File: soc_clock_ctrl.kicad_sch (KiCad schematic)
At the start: 19 parts, among them U1 MCIMX6Y2DVM09AB

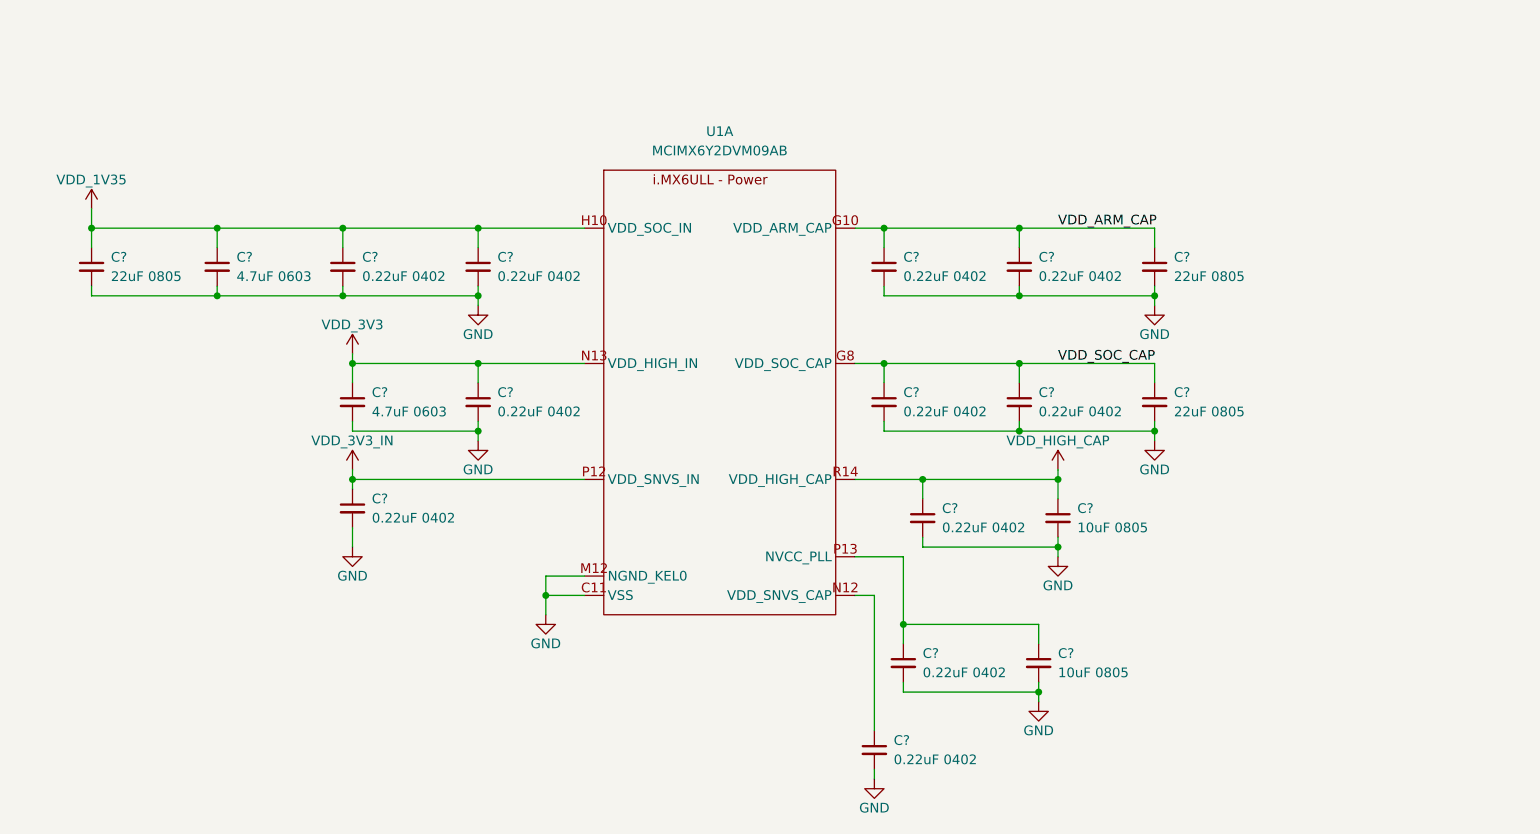
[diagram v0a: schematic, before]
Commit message: Core power; clock/ctrl
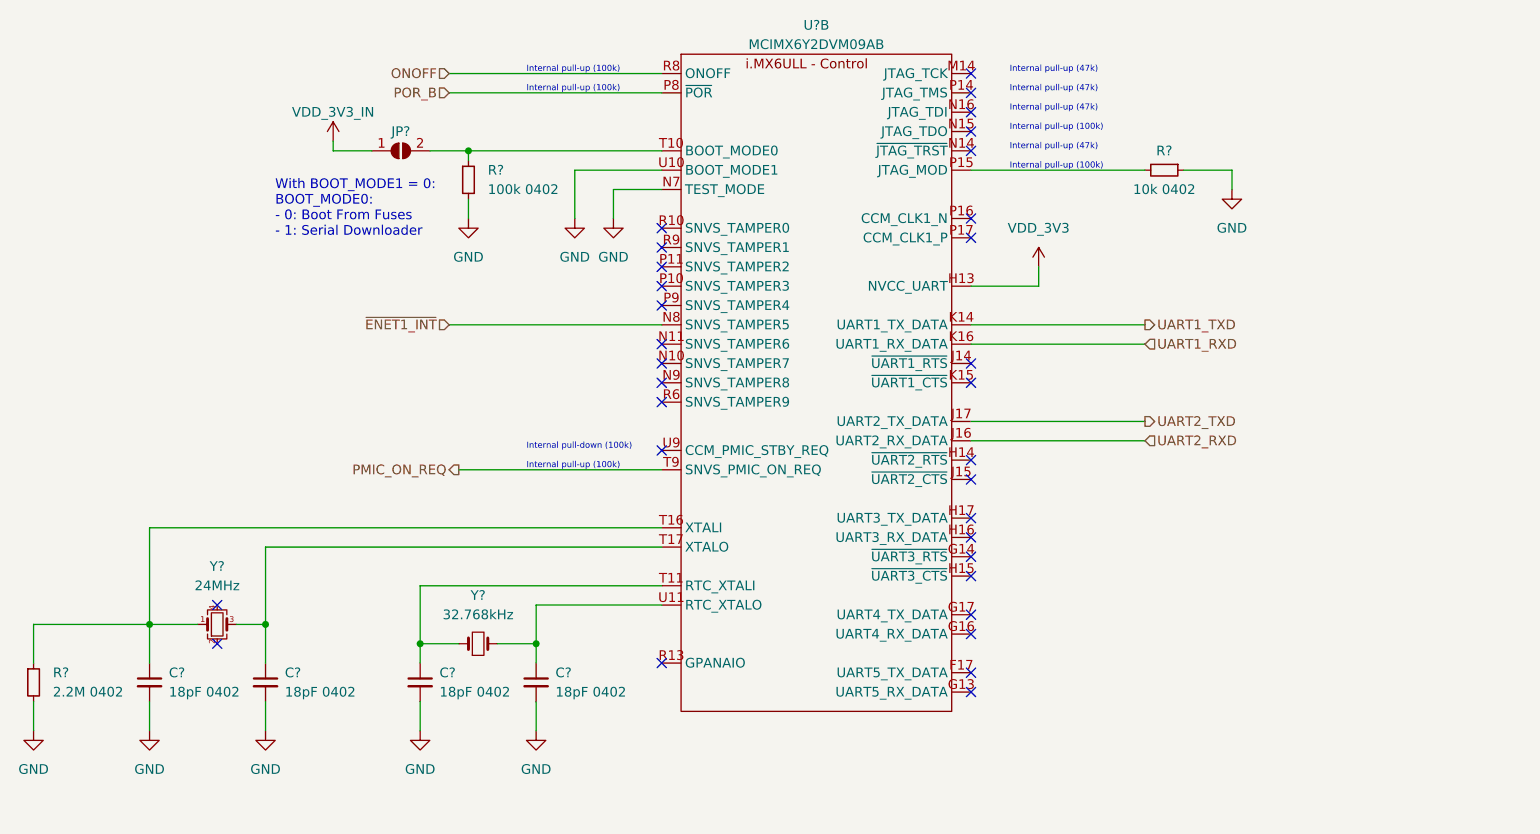
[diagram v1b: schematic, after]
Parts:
- removed C? (x11): 0.22uF 0402, symbol Device:C_Small
- removed C? (x2): 10uF 0805, symbol Device:C_Small
- removed C? (x2): 4.7uF 0603, symbol Device:C_Small
- removed C? (x3): 22uF 0805, symbol Device:C_Small
- removed U1: MCIMX6Y2DVM09AB, symbol catfood:MCIMX6YxxVMxxxx
- added C? (x4): 18pF 0402, symbol Device:C_Small
- added JP?: SolderJumper_2_Open, symbol Jumper:SolderJumper_2_Open
- added R?: 10k 0402, symbol Device:R_Small
- added R?: 2.2M 0402, symbol Device:R_Small
- added R?: 100k 0402, symbol Device:R_Small
- added U?: MCIMX6Y2DVM09AB, symbol catfood:MCIMX6YxxVMxxxx
- added Y?: 24MHz, symbol Device:Crystal_GND24_Small
- added Y?: 32.768kHz, symbol Device:Crystal_Small
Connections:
- net GND: now also C?.2, C?.2, C?.2, C?.2, R?.1, R?.2, R?.2, U?.N7 (TEST_MODE), U?.U10 (BOOT_MODE1)
- net VDD_3V3: now also U?.H13 (NVCC_UART)
- net VDD_3V3_IN: now also JP?.1 (A)
- new net: C?.1, R?.1, U?.T16 (XTALI), Y?.1
- new net: C?.1, U?.T17 (XTALO), Y?.3
- new net: R?.2, U?.P15 (JTAG_MOD)
- new net: JP?.2 (B), R?.1, U?.T10 (BOOT_MODE0)
- new net: C?.1, U?.T11 (RTC_XTALI), Y?.1
- new net: C?.1, U?.U11 (RTC_XTALO), Y?.2
- new net ONOFF: U?.R8 (ONOFF)
- new net PMIC_ON_REQ: U?.T9 (SNVS_PMIC_ON_REQ)
- new net POR_B: U?.P8 (~{POR})
- new net UART1_RXD: U?.K16 (UART1_RX_DATA)
- new net UART1_TXD: U?.K14 (UART1_TX_DATA)
- new net UART2_RXD: U?.J16 (UART2_RX_DATA)
- new net UART2_TXD: U?.J17 (UART2_TX_DATA)
- new net ~{ENET1_INT}: U?.N8 (SNVS_TAMPER5)
- no-connect marks 0 -> 32
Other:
- note added: "Internal pull-down (100k)"
- note added: "Internal pull-up (100k)"
- note added: "Internal pull-up (47k)"
- note added: "With BOOT_MODE1 = 0: BOOT_MODE0: - 0: Boot From Fuses - 1: Serial Downloader"
- company: Ian Kilgore -> (none)
- title: catfood -> (none)

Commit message: Ethernet schematic
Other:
- company: (none) -> Ian Kilgore
- title: (none) -> catfood
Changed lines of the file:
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@@
 (kicad_sch (version 20211123) (generator eeschema)
-  (paper "A4")
+  (paper "USLetter")
+  (title_block
+    (title "catfood")
+    (company "Ian Kilgore")
+  )
   (junction (at 118.11 124.46) (diameter 0) (color 0 0 0 0)
   )

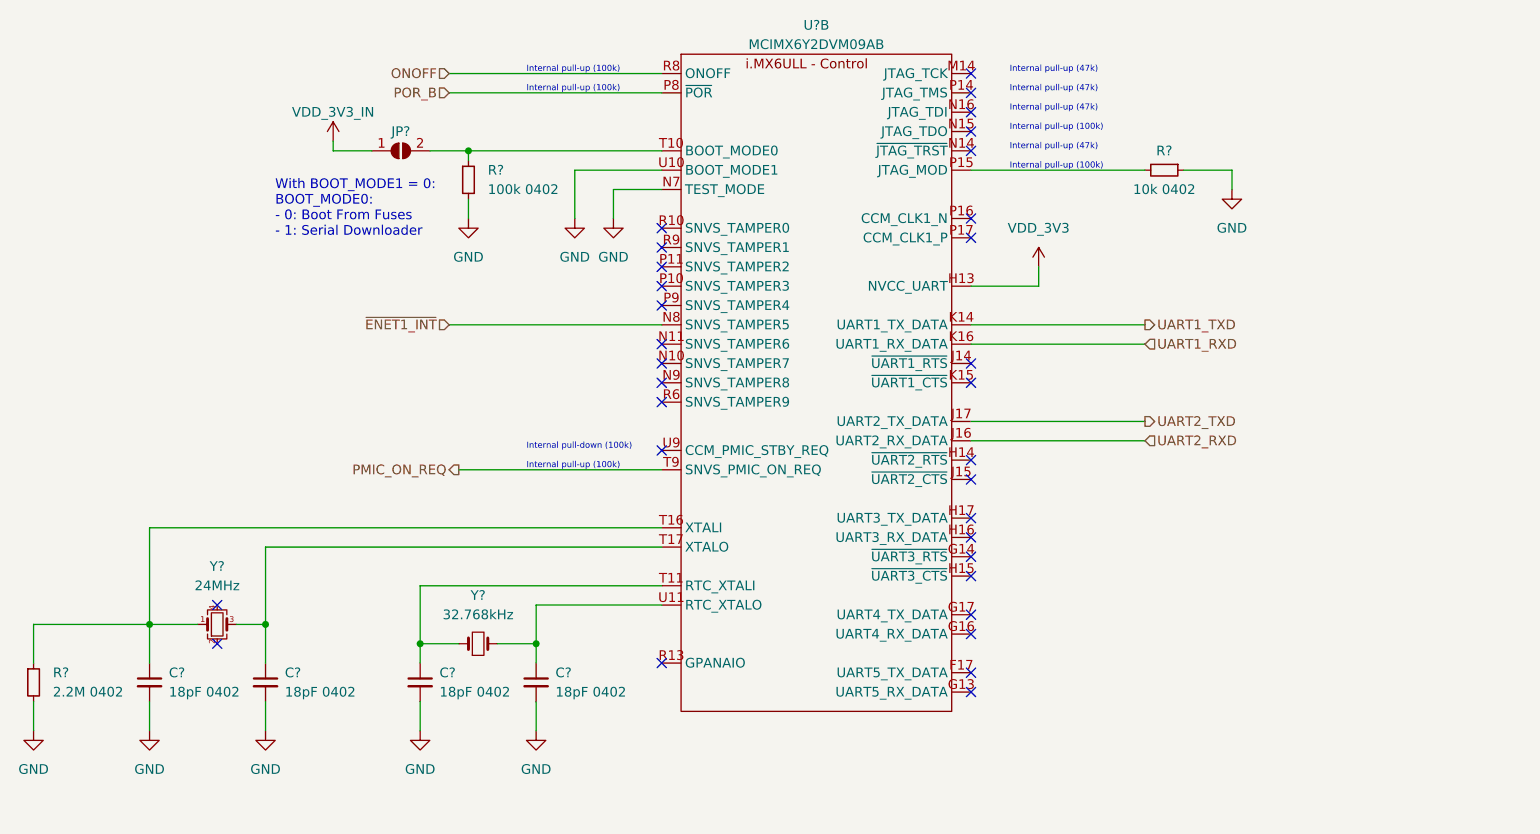
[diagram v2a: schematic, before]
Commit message: Ethernet TVS, UART headers
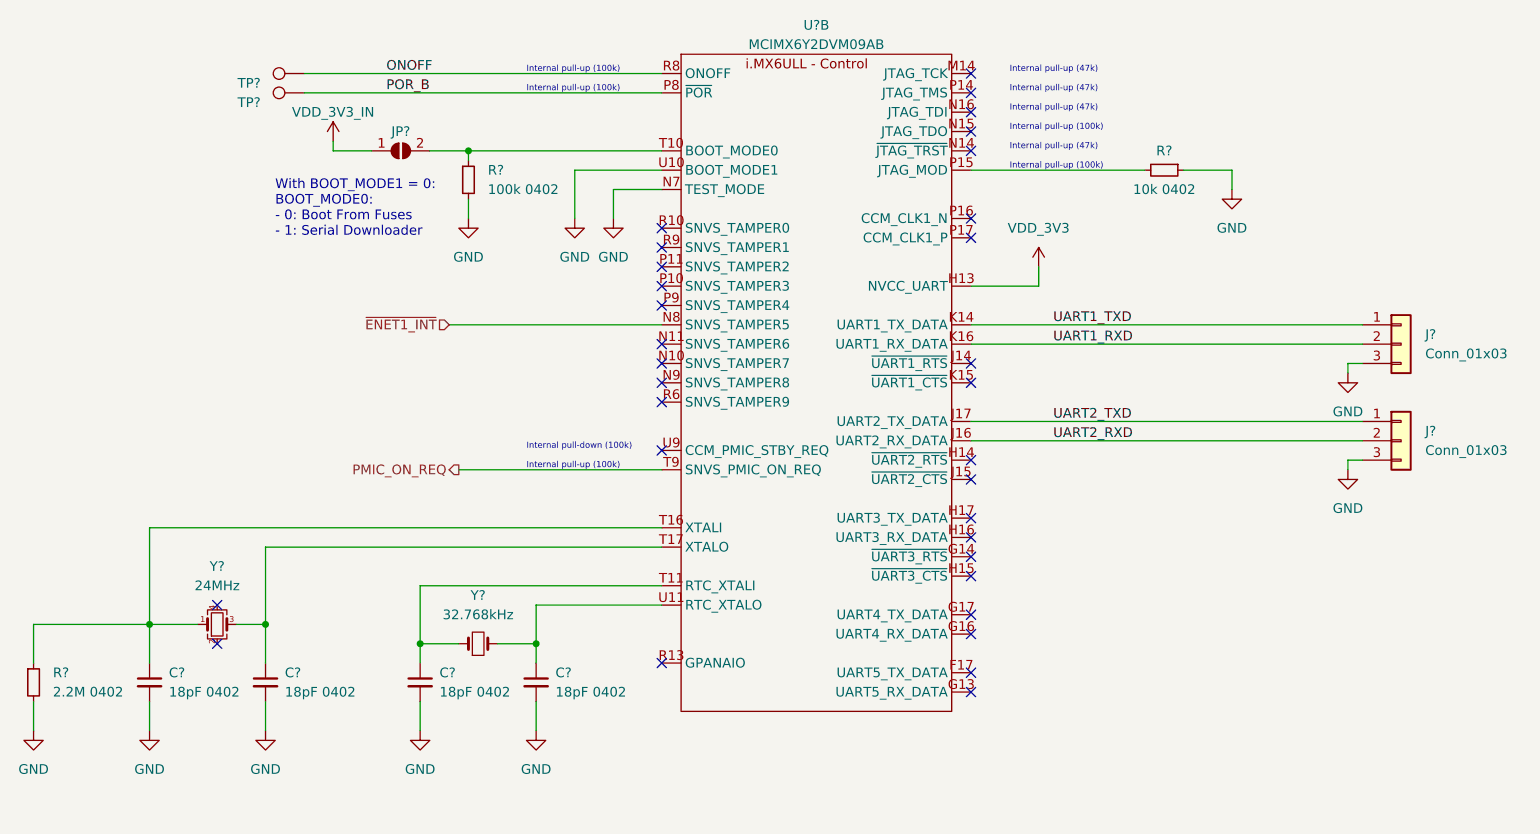
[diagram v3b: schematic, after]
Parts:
- added J? (x2): Conn_01x03, symbol Connector_Generic:Conn_01x03
- added TP? (x2): TestPoint, symbol Connector:TestPoint
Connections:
- net GND: now also J?.3 (Pin_3), J?.3 (Pin_3)
- net ONOFF: now also TP?.1
- net POR_B: now also TP?.1
- net UART1_RXD: now also J?.2 (Pin_2)
- net UART1_TXD: now also J?.1 (Pin_1)
- net UART2_RXD: now also J?.2 (Pin_2)
- net UART2_TXD: now also J?.1 (Pin_1)
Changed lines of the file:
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@@
+    (stroke (width 0) (type default) (color 0 0 0 0))
+  )
+  (wire (pts (xy 226.695 87.63) (xy 224.79 87.63))
     (stroke (width 0) (type default) (color 0 0 0 0))
   )
@@
     (stroke (width 0) (type default) (color 0 0 0 0))
   )
+  (wire (pts (xy 224.79 87.63) (xy 224.79 88.9))
+    (stroke (width 0) (type default) (color 0 0 0 0))
+  )
   (wire (pts (xy 52.07 127) (xy 52.07 121.92))
     (stroke (width 0) (type default) (color 0 0 0 0))
@@
     (stroke (width 0) (type default) (color 0 0 0 0))
   )
+  (wire (pts (xy 224.79 100.33) (xy 224.79 101.6))
+    (stroke (width 0) (type default) (color 0 0 0 0))
+  )
   (wire (pts (xy 104.14 59.69) (xy 109.22 59.69))
     (stroke (width 0) (type default) (color 0 0 0 0))
@@
     (stroke (width 0) (type default) (color 0 0 0 0))
   )
-  (wire (pts (xy 175.26 97.79) (xy 198.12 97.79))
-    (stroke (width 0) (type default) (color 0 0 0 0))
-  )
-  (wire (pts (xy 175.26 95.25) (xy 198.12 95.25))
+  (wire (pts (xy 175.26 97.79) (xy 226.695 97.79))
+    (stroke (width 0) (type default) (color 0 0 0 0))
+  )
+  (wire (pts (xy 175.26 95.25) (xy 226.695 95.25))
     (stroke (width 0) (type default) (color 0 0 0 0))
   )
@@
     (stroke (width 0) (type default) (color 0 0 0 0))
   )
-  (wire (pts (xy 106.68 52.07) (xy 134.62 52.07))
+  (wire (pts (xy 87.63 52.07) (xy 134.62 52.07))
     (stroke (width 0) (type default) (color 0 0 0 0))
   )
@@
     (stroke (width 0) (type default) (color 0 0 0 0))
   )
-  (wire (pts (xy 175.26 82.55) (xy 198.12 82.55))
+  (wire (pts (xy 175.26 82.55) (xy 226.695 82.55))
     (stroke (width 0) (type default) (color 0 0 0 0))
   )
@@
     (stroke (width 0) (type default) (color 0 0 0 0))
   )
-  (wire (pts (xy 106.68 49.53) (xy 134.62 49.53))
+  (wire (pts (xy 87.63 49.53) (xy 134.62 49.53))
     (stroke (width 0) (type default) (color 0 0 0 0))
   )
@@
     (stroke (width 0) (type default) (color 0 0 0 0))
   )
-  (wire (pts (xy 175.26 85.09) (xy 198.12 85.09))
+  (wire (pts (xy 175.26 85.09) (xy 226.695 85.09))
+    (stroke (width 0) (type default) (color 0 0 0 0))
+  )
+  (wire (pts (xy 226.695 100.33) (xy 224.79 100.33))
     (stroke (width 0) (type default) (color 0 0 0 0))
   )
@@
     (effects (font (size 0.8 0.8)) (justify left bottom))
   )
-  (hierarchical_label "UART1_RXD" (shape input) (at 198.12 85.09 0)
-    (effects (font (size 1.27 1.27)) (justify left))
-  )
-  (hierarchical_label "UART2_RXD" (shape input) (at 198.12 97.79 0)
-    (effects (font (size 1.27 1.27)) (justify left))
-  )
-  (hierarchical_label "ONOFF" (shape input) (at 106.68 49.53 180)
-    (effects (font (size 1.27 1.27)) (justify right))
+  (label "UART2_RXD" (at 186.055 97.79 0)
+    (effects (font (size 1.27 1.27)) (justify left bottom))
+  )
+  (label "UART1_TXD" (at 186.055 82.55 0)
+    (effects (font (size 1.27 1.27)) (justify left bottom))
+  )
+  (label "ONOFF" (at 98.425 49.53 0)
+    (effects (font (size 1.27 1.27)) (justify left bottom))
+  )
+  (label "UART2_TXD" (at 186.055 95.25 0)
+    (effects (font (size 1.27 1.27)) (justify left bottom))
+  )
+  (label "POR_B" (at 98.425 52.07 0)
+    (effects (font (size 1.27 1.27)) (justify left bottom))
+  )
+  (label "UART1_RXD" (at 186.055 85.09 0)
+    (effects (font (size 1.27 1.27)) (justify left bottom))
   )
   (hierarchical_label "PMIC_ON_REQ" (shape output) (at 107.95 101.6 180)
-    (effects (font (size 1.27 1.27)) (justify right))
-  )
-  (hierarchical_label "UART2_TXD" (shape output) (at 198.12 95.25 0)
-    (effects (font (size 1.27 1.27)) (justify left))
-  )
-  (hierarchical_label "UART1_TXD" (shape output) (at 198.12 82.55 0)
-    (effects (font (size 1.27 1.27)) (justify left))
-  )
-  (hierarchical_label "POR_B" (shape input) (at 106.68 52.07 180)
     (effects (font (size 1.27 1.27)) (justify right))
   )
@@
     (pin "2")
   )
+  (symbol (lib_id "power:GND") (at 224.79 101.6 0) (unit 1)
+    (in_bom yes) (on_board yes) (fields_autoplaced)
+    (property "Reference" "#PWR?" (id 0) (at 224.79 107.95 0)
+      (effects (font (size 1.27 1.27)) hide)
+    )
+    (property "Value" "GND" (id 1) (at 224.79 106.68 0))
+    (property "Footprint" "" (id 2) (at 224.79 101.6 0)
+      (effects (font (size 1.27 1.27)) hide)
+    )
+    (property "Datasheet" "" (id 3) (at 224.79 101.6 0)
+      (effects (font (size 1.27 1.27)) hide)
+    )
+    (pin "1")
+  )
   (symbol (lib_id "catfood:VDD_3V3") (at 184.15 74.93 0) (unit 1)
     (in_bom yes) (on_board yes) (fields_autoplaced)
@@
     )
     (pin "1")
+  )
+  (symbol (lib_id "Connector:TestPoint") (at 87.63 49.53 90) (unit 1)
+    (in_bom yes) (on_board yes) (fields_autoplaced)
+    (property "Reference" "TP?" (id 0) (at 81.915 50.8001 90)
+      (effects (font (size 1.27 1.27)) (justify left))
+    )
+    (property "Value" "TestPoint" (id 1) (at 81.915 48.2601 90)
+      (effects (font (size 1.27 1.27)) (justify left) hide)
+    )
+    (property "Footprint" "" (id 2) (at 87.63 44.45 0)
+      (effects (font (size 1.27 1.27)) hide)
+    )
+    (property "Datasheet" "~" (id 3) (at 87.63 44.45 0)
+      (effects (font (size 1.27 1.27)) hide)
+    )
+    (pin "1")
+  )
+  (symbol (lib_id "power:GND") (at 224.79 88.9 0) (unit 1)
+    (in_bom yes) (on_board yes) (fields_autoplaced)
+    (property "Reference" "#PWR?" (id 0) (at 224.79 95.25 0)
+      (effects (font (size 1.27 1.27)) hide)
+    )
+    (property "Value" "GND" (id 1) (at 224.79 93.98 0))
+    (property "Footprint" "" (id 2) (at 224.79 88.9 0)
+      (effects (font (size 1.27 1.27)) hide)
+    )
+    (property "Datasheet" "" (id 3) (at 224.79 88.9 0)
+      (effects (font (size 1.27 1.27)) hide)
+    )
+    (pin "1")
+  )
+  (symbol (lib_id "Connector_Generic:Conn_01x03") (at 231.775 97.79 0) (unit 1)
+    (in_bom yes) (on_board yes) (fields_autoplaced)
+    (property "Reference" "J?" (id 0) (at 234.95 96.5199 0)
+      (effects (font (size 1.27 1.27)) (justify left))
+    )
+    (property "Value" "Conn_01x03" (id 1) (at 234.95 99.0599 0)
+      (effects (font (size 1.27 1.27)) (justify left))
+    )
+    (property "Footprint" "" (id 2) (at 231.775 97.79 0)
+      (effects (font (size 1.27 1.27)) hide)
+    )
+    (property "Datasheet" "~" (id 3) (at 231.775 97.79 0)
+      (effects (font (size 1.27 1.27)) hide)
+    )
+    (pin "1")
+    (pin "2")
+    (pin "3")
   )
   (symbol (lib_id "power:GND") (at 109.22 68.58 0) (unit 1)
@@
     (pin "2")
   )
+  (symbol (lib_id "Connector_Generic:Conn_01x03") (at 231.775 85.09 0) (unit 1)
+    (in_bom yes) (on_board yes) (fields_autoplaced)
+    (property "Reference" "J?" (id 0) (at 234.95 83.8199 0)
+      (effects (font (size 1.27 1.27)) (justify left))
+    )
+    (property "Value" "Conn_01x03" (id 1) (at 234.95 86.3599 0)
+      (effects (font (size 1.27 1.27)) (justify left))
+    )
+    (property "Footprint" "" (id 2) (at 231.775 85.09 0)
+      (effects (font (size 1.27 1.27)) hide)
+    )
+    (property "Datasheet" "~" (id 3) (at 231.775 85.09 0)
+      (effects (font (size 1.27 1.27)) hide)
+    )
+    (pin "1")
+    (pin "2")
+    (pin "3")
+  )
   (symbol (lib_id "power:GND") (at 52.07 135.89 0) (unit 1)
     (in_bom yes) (on_board yes) (fields_autoplaced)
@@
       (effects (font (size 1.27 1.27)) hide)
     )
+    (pin "1")
+  )
+  (symbol (lib_id "Connector:TestPoint") (at 87.63 52.07 90) (unit 1)
+    (in_bom yes) (on_board yes) (fields_autoplaced)
+    (property "Reference" "TP?" (id 0) (at 81.915 53.3401 90)
+      (effects (font (size 1.27 1.27)) (justify left))
+    )
+    (property "Value" "TestPoint" (id 1) (at 81.915 50.8001 90)
+      (effects (font (size 1.27 1.27)) (justify left) hide)
+    )
+    (property "Footprint" "" (id 2) (at 87.63 46.99 0)
+      (effects (font (size 1.27 1.27)) hide)
+    )
+    (property "Datasheet" "~" (id 3) (at 87.63 46.99 0)
+      (effects (font (size 1.27 1.27)) hide)
+    )
